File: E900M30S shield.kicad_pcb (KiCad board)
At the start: 2 copper layers, 55 x 40 mm, 5 parts, among them J1 Conn10, J2 Conn02, U1 E22-900M30S

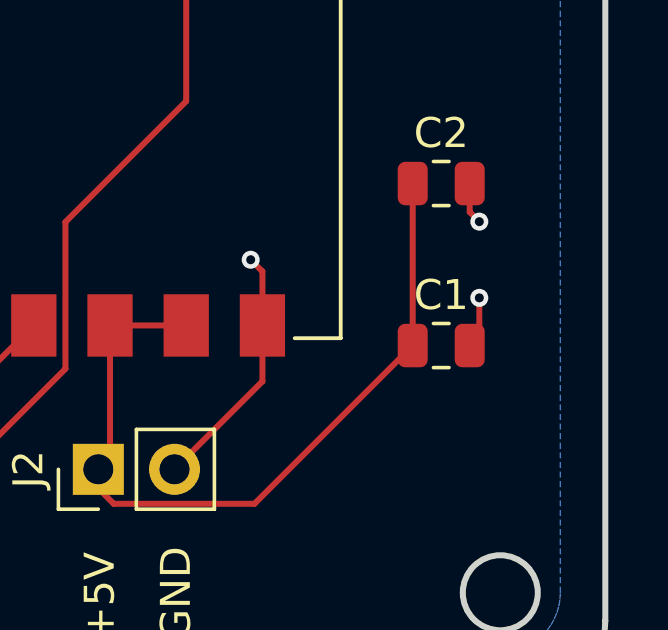
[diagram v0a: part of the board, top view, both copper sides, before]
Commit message: Update cap values
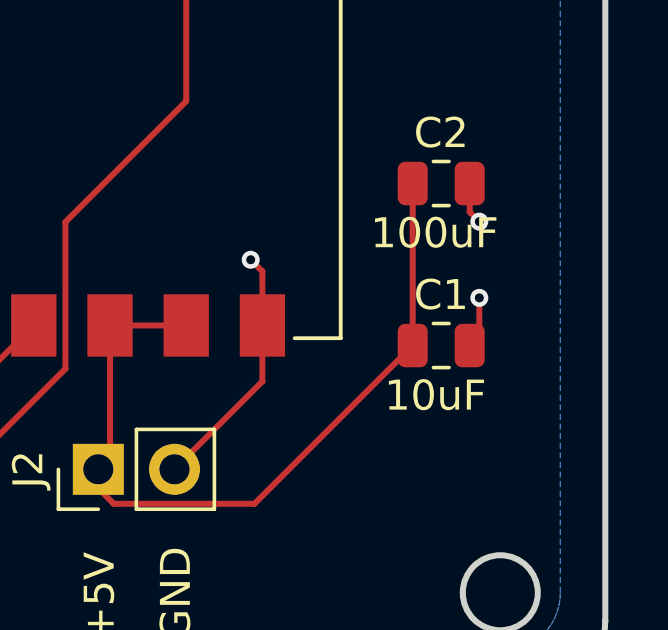
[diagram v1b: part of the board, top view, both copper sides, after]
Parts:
- C1: value 10uf -> 10uF
- C2: value 100uf -> 100uF
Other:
- board text added: "100uF"
- board text added: "10uF"
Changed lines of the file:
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@@
 		(property ki_fp_filters "Connector_JST:JST_EH_S10B-EH_1x10_P2.50mm_Horizontal")
 		(sheetname "Root")
-		(sheetfile "E900T30S shield.kicad_sch")
+		(sheetfile "E900M30S shield.kicad_sch")
 		(attr through_hole)
 		(fp_line
@@
 		(property ki_fp_filters "Connector_JST:JST_EH_S2B-EH_1x02_P2.50mm_Horizontal")
 		(sheetname "Root")
-		(sheetfile "E900T30S shield.kicad_sch")
+		(sheetfile "E900M30S shield.kicad_sch")
 		(attr through_hole)
 		(fp_line
@@
 			)
 		)
-		(property "Value" "10uf"
+		(property "Value" "10uF"
 			(at 0 1.68 0)
 			(layer "F.Fab")
@@
 		(property ki_fp_filters "Capacitor_THT:C_Rect_L7.0mm_W3.5mm_P5.00mm Capacitor_THT:C_Rect_L7.0mm_W4.5mm_P5.00mm Capacitor_THT:C_Rect_L29.0mm_W7.6mm_P27.50mm_MKT Capacitor_THT:C_Rect_L24.0mm_W7.0mm_P22.50mm_MKT Capacitor_THT:C_Rect_L11.5mm_W5.0mm_P10.00mm_MKT Capacitor_THT:C_Rect_L9.0mm_W3.6mm_P7.50mm_MKT")
 		(sheetname "Root")
-		(sheetfile "E900T30S shield.kicad_sch")
+		(sheetfile "E900M30S shield.kicad_sch")
 		(attr smd)
 		(fp_line
@@
 		)
 		(sheetname "Root")
-		(sheetfile "E900T30S shield.kicad_sch")
+		(sheetfile "E900M30S shield.kicad_sch")
 		(attr smd)
 		(fp_line
@@
 			)
 		)
-		(property "Value" "100uf"
+		(property "Value" "100uF"
 			(at 0 1.68 0)
 			(layer "F.Fab")
@@
 		(property ki_fp_filters "Capacitor_THT:C_Rect_L7.0mm_W3.5mm_P5.00mm Capacitor_THT:C_Rect_L7.0mm_W4.5mm_P5.00mm Capacitor_THT:C_Rect_L29.0mm_W7.6mm_P27.50mm_MKT Capacitor_THT:C_Rect_L24.0mm_W7.0mm_P22.50mm_MKT Capacitor_THT:C_Rect_L11.5mm_W5.0mm_P10.00mm_MKT Capacitor_THT:C_Rect_L9.0mm_W3.6mm_P7.50mm_MKT")
 		(sheetname "Root")
-		(sheetfile "E900T30S shield.kicad_sch")
+		(sheetfile "E900M30S shield.kicad_sch")
 		(attr smd)
 		(fp_line
@@
 		(layer "Edge.Cuts")
 	)
+	(gr_text "10uF"
+		(at 156.854639 127.038337 0)
+		(layer "F.SilkS")
+		(effects
+			(font
+				(size 1 1)
+				(thickness 0.1)
+			)
+			(justify left bottom)
+		)
+	)
 	(gr_text "MOSI"
 		(at 125.095 134.62 90)
@@
 		(layer "F.SilkS")
 		(effects
+			(font
+				(size 1 1)
+				(thickness 0.1)
+			)
+			(justify left bottom)
+		)
+	)
+	(gr_text "100uF"
+		(at 156.39287 121.624884 0)
+		(layer "F.SilkS")
+		(effects

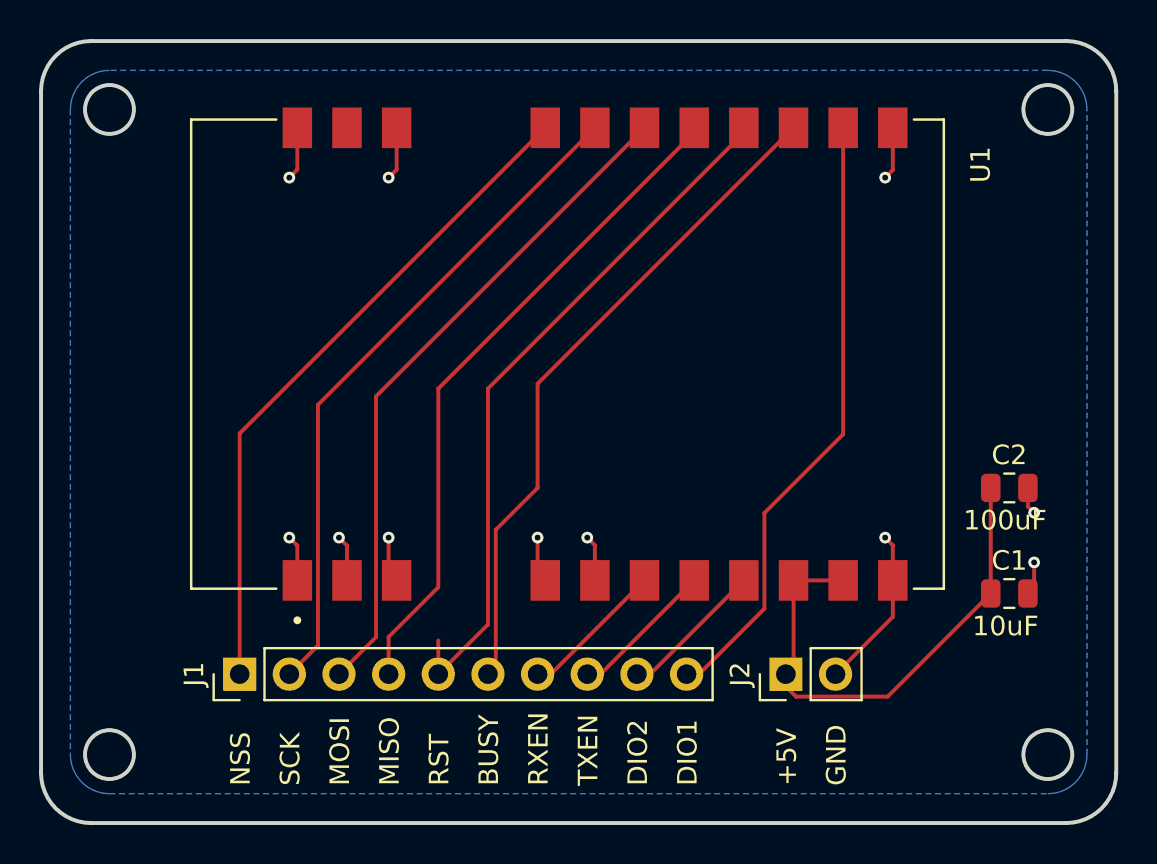
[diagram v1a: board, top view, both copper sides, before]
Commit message: Rearrange decoupling caps Front side ground plane Double width power traces
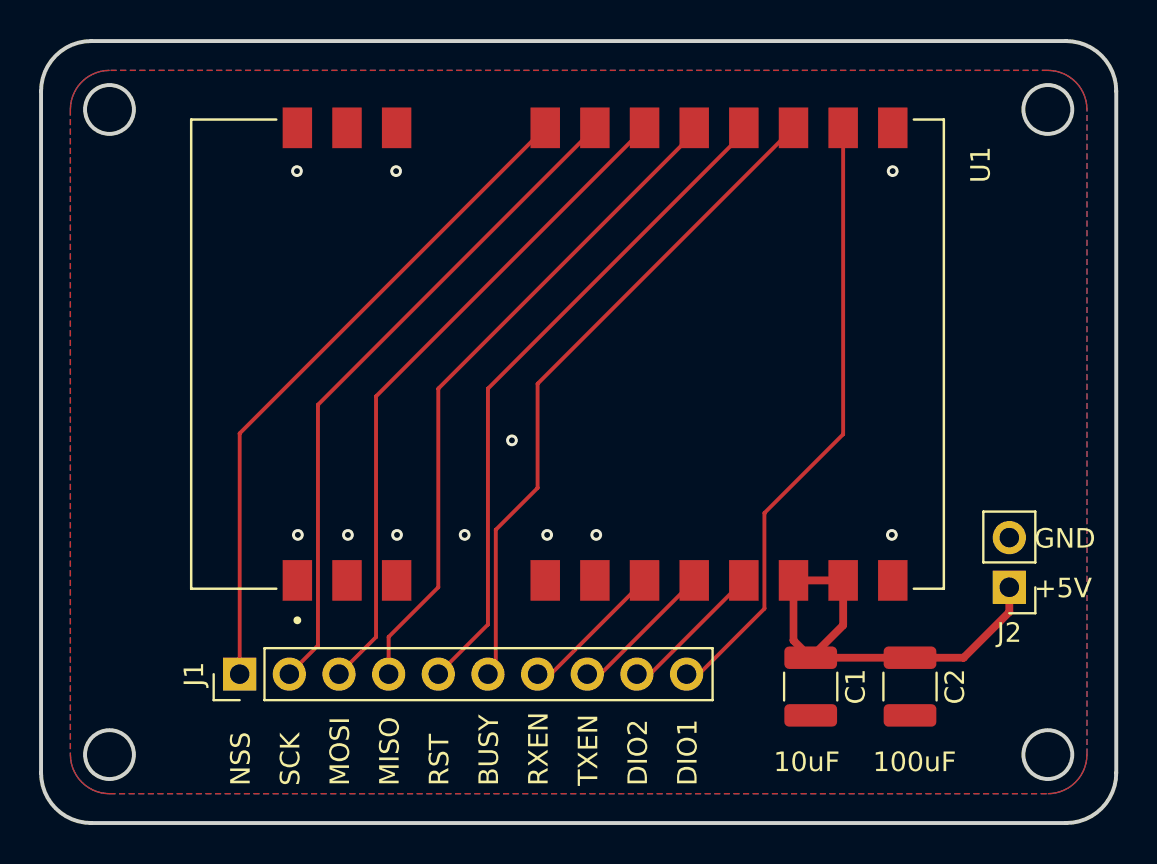
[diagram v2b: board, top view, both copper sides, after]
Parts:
- C1, C2: footprint Capacitor_SMD:C_0805_2012Metric -> Capacitor_SMD:C_1210_3225Metric
- moved J2 12.3 mm to (158.8, 124.5), turned to 180 degrees
- moved C2 11.4 mm to (153.7, 129.5), turned to -90 degrees
- moved C1 11.2 mm to (148.6, 129.5), turned to -90 degrees
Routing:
- net GND: track 31.4 -> 1.13 mm
- net +5V: track 26.4 -> 23.9 mm
- net RST: track 36.1 -> 34.4 mm
- added copper zone on F.Cu, net GND
